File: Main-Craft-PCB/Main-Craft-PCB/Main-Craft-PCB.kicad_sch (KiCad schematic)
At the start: 220 parts, among them J1 Conn_01x10, J1 UART_1, J10 SOL_2, J11 PWR_IN, J12 SOL_3, J13 SOL_4, J15 VESC_1, J16 VESC_2, J17 VESC_3, J18 VESC_4, J19 S500_1, J2 UART_2, J20 S500_2, J21 S500_3, J22 S500_4, J23 LEDS, J24 LEDS, J25 LEDS, J26 LEDS, J3 UART_3, J4 UART_4, J5 RELAY_1, J6 RELAY_2, J7 RELAY_3, J8 RELAY_3, J9 SOL_1, Q1 TIP120, Q10 S9013, Q11 S9013, Q12 S9013, Q13 S9013, Q14 S9013, Q16 S9013, Q2 TIP120, Q25 IRFR9014PBF, Q3 TIP120, Q4 TIP120, Q5 S9013, Q6 S9013, Q7 S9013, Q8 S9013, Q9 S9013, U10 BFU590GX, U10 ZLDO1117G50TA, U2 NUCLEO144-F429ZI, U3 ESP8266, U4 LM358DR2G, U4 SN74LV4052, U5 74HC14, U5 LM358, U8 Pi Pico, U9 74HC14, U9 ZSR330GTA

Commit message: Finish add all footprints and components
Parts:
- AS_DEC_SW1: footprint My_library:1Ms1T1B1M1QE -> My_library:JS202011SCQN
- C1: footprint (none) -> Capacitor_SMD:CP_Elec_10x10.5
- C28, C29, C33, C34: value C -> 100nF; footprint (none) -> Capacitor_SMD:C_0603_1608Metric
- D11, D12, D19, D20, D21, D22, D23, D24: value BLUE -> RED
- D28: value BLUE -> GREEN
- D29: value BLUE -> YELLOW
- D_UP1: footprint Button_Switch_SMD:SW_Push_1P1T_NO_6x6mm_H9.5mm -> My_library:12AWG_PWR_IN
- J1, J2, J3, J4: footprint (none) -> My_library:Conn_01x04_MOLEX
- J10, J12, J13, J15, J16, J17, J18, J19, J20, J21, J22, J5, J6, J7, J8, J9: footprint (none) -> My_library:Conn_01x03_MOLEX
- J11: footprint (none) -> My_library:12AWG_PWR_IN
- J23, J24, J25, J26: footprint (none) -> Connector_PinHeader_2.54mm:PinHeader_1x02_P2.54mm_Vertical
- R33, R34, R43, R44, R47, R48, R51, R52, R86: value 1K -> 150R
- R61: value 1K -> 2K2
- RV10, RV11, RV12, RV9: value R_POT -> 20K; footprint (none) -> My_library:Variable_Resistor
- U2: footprint My_library:MODULE_NUCLEO-F429ZI_JUST_PINS -> My_library:MODULE_NUCLEO-F429ZI
- U3: footprint (none) -> My_library:ESP-8266
- U4: footprint (none) -> Package_SO:SOIC-16_4.55x10.3mm_P1.27mm
- U5: value LM358 -> LM358DR2G; footprint (none) -> Package_SO:SOP-8_3.76x4.96mm_P1.27mm
- U8: footprint (none) -> My_library:Pi_Pico
- U9: footprint (none) -> Package_SO:SO-14_3.9x8.65mm_P1.27mm
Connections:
- net +12V: now also U2.24 (VIN)
- net RESET: now also U2.14 (~{RST})
- removed net LED_1: R25.2, R26.2, R41.2, R42.2, R45.2, R46.2, R49.2, R50.2
- removed net TRIM_POT_?: C28.1, C29.1, C33.1, C34.1, RV10.2, RV11.2, RV12.2, RV9.2
- new net SENS_1: R25.2
- new net SENS_2: R41.2
- new net SENS_3: R45.2
- new net SENS_4: R49.2
- new net SENS_5: R26.2
- new net SENS_6: R42.2
- new net SENS_7: R46.2
- new net SENS_8: R50.2
- new net TRIM_POT_1: C28.1, RV9.2
- new net TRIM_POT_2: C33.1, RV11.2
- new net TRIM_POT_3: C29.1, RV10.2
- new net TRIM_POT_4: C34.1, RV12.2
- no-connect marks 51 -> 60
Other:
- moved on the sheet: U3, U8

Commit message: Start PCB Layout Place Most of Components
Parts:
- removed R89: 2K2, Resistor_SMD:R_0603_1608Metric, symbol Device:R
- removed R91: 10K, Resistor_SMD:R_0603_1608Metric, symbol Device:R
- removed RESET1: SW_SPST, Button_Switch_SMD:SW_Push_1P1T_NO_6x6mm_H9.5mm, symbol Switch:SW_SPST
- D_UP1: footprint My_library:12AWG_PWR_IN -> Button_Switch_SMD:SW_Push_1P1T_NO_6x6mm_H9.5mm
- J1: footprint Connector_PinHeader_1.27mm:PinHeader_1x10_P1.27mm_Vertical -> Connector_PinSocket_2.54mm:PinSocket_1x10_P2.54mm_Vertical
- J10, J12, J13, J9: footprint My_library:Conn_01x03_MOLEX -> My_library:Conn_01x02_MOLEX
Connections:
- net BTN_1: now also U2.38 (PC0)
- net BTN_2: now also U2.45 (PD7)
- net BTN_3: now also U2.43 (PD6)
- net BTN_4: now also U2.41 (PD5)
- net BTN_5: now also U2.39 (PD4)
- net BTN_6: now also U2.40 (PD3)
- net CLK_1: now also U2.11 (PF7)
- net CLK_2: now also U2.46 (PE2)
- net CON_INPUT: now also U2.114 (PF10)
- net DEBUG_1: now also U2.121 (PE12)
- net DEBUG_2: now also U2.123 (PE14)
- net DEBUG_3: now also U2.125 (PE15)
- net I2C_ESP_SCl: now also U2.75 (PB8)
- net I2C_ESP_SDA: now also U2.77 (PB9)
- net I2C_PICO_SCl: now also U2.97 (PB10)
- net I2C_PICO_SDA: now also U2.90 (PB11)
- net LOW_VOLT_1: now also U2.94 (PB2)
- net LOW_VOLT_2: now also U2.117 (PD11)
- net LOW_VOLT_3: now also U2.28 (ETH_REF_CLK/PA0)
- net LOW_VOLT_4: now also U2.136 (PE0)
- net MISO_1: now also U2.56 (PF9)
- net MISO_2: now also U2.50 (PE5)
- net MOSI_1: now also U2.54 (PF8)
- net MOSI_2: now also U2.62 (PE6)
- net RELAY_1: now also U2.52 (PF2)
- net RELAY_2: now also U2.57 (PD0)
- net RELAY_3: now also U2.55 (PD1)
- net RELAY_4: now also U2.59 (PG0)
- net S500_1: now also U2.96 (PB1)
- net S500_2: now also U2.89 (PB6)
- net S500_3: now also U2.113 (PD13)
- net S500_4: now also U2.115 (PD12)
- net SENS_1: now also U2.131 (PF12)
- net SENS_2: now also U2.129 (PF13)
- net SENS_3: now also U2.124 (PE9)
- net SENS_4: now also U2.128 (PE11)
- net SENS_5: now also U2.122 (PF14)
- net SENS_6: now also U2.127 (PE13)
- net SENS_7: now also U2.132 (PF15)
- net SENS_8: now also U2.133 (PG14)
- net SOL_1: now also U2.63 (PG9)
- net SOL_2: now also U2.112 (PE8)
- net SOL_3: now also U2.116 (PE7)
- net SOL_4: now also U2.119 (PE10)
- net SW_1_DOWN: now also U2.2 (PC11)
- net SW_1_UP: now also U2.1 (PC10)
- net SW_2_DOWN: now also U2.4 (PD2)
- net SW_2_UP: now also U2.3 (PC12)
- net SW_3_DOWN: now also U2.44 (PG3)
- net SW_3_UP: now also U2.42 (PG2)
- net TRIM_POT_1: now also U2.32 (PA4)
- net TRIM_POT_2: now also U2.83 (PA5)
- net TRIM_POT_3: now also U2.85 (PA6)
- net TRIM_POT_4: now also U2.87 (ETH_CRS_DV/PA7)
- net VESC_1: now also U2.109 (PA3)
- net VESC_2: now also U2.74 (PC8)
- net VESC_3: now also U2.73 (PC9)
- net VESC_4: now also U2.99 (PB4)
- no-connect marks 60 -> 116
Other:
- moved on the sheet: D11, D12, D19, D20, D21, D22, D23, D24, Q10, Q11, Q12, Q5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

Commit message: Continue PCB
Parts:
- added J23: BAT_IN, My_library:Conn_01x04_MOLEX, symbol Connector_Generic:Conn_01x04
- renumbered C28 to C26, C29 to C27, C33 to C31, C34 to C32, C1 to C36, J20 to J10, J21 to J11, J22 to J12, J9 to J13, J10 to J14, J5 to J15, J6 to J16, J7 to J17, J8 to J18, J12 to J19, J13 to J20, J11 to J21, J15 to J24, J16 to J25, J17 to J26, J18 to J27, J23 to J5, J24 to J6, J25 to J7, J26 to J8, J19 to J9, R3 to R1, R4 to R2, R25 to R24, R26 to R25, R33 to R32, R34 to R33, R2 to R40, R58 to R57, R60 to R58, R61 to R59, R63 to R61, R64 to R62, U8 to U2, U9 to U8
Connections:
- net BATT_1_IN: now also J23.1 (Pin_1)
- net BATT_2_IN: now also J23.2 (Pin_2)
- net BATT_3_IN: now also J23.3 (Pin_3)
- net BATT_4_IN: now also J23.4 (Pin_4)

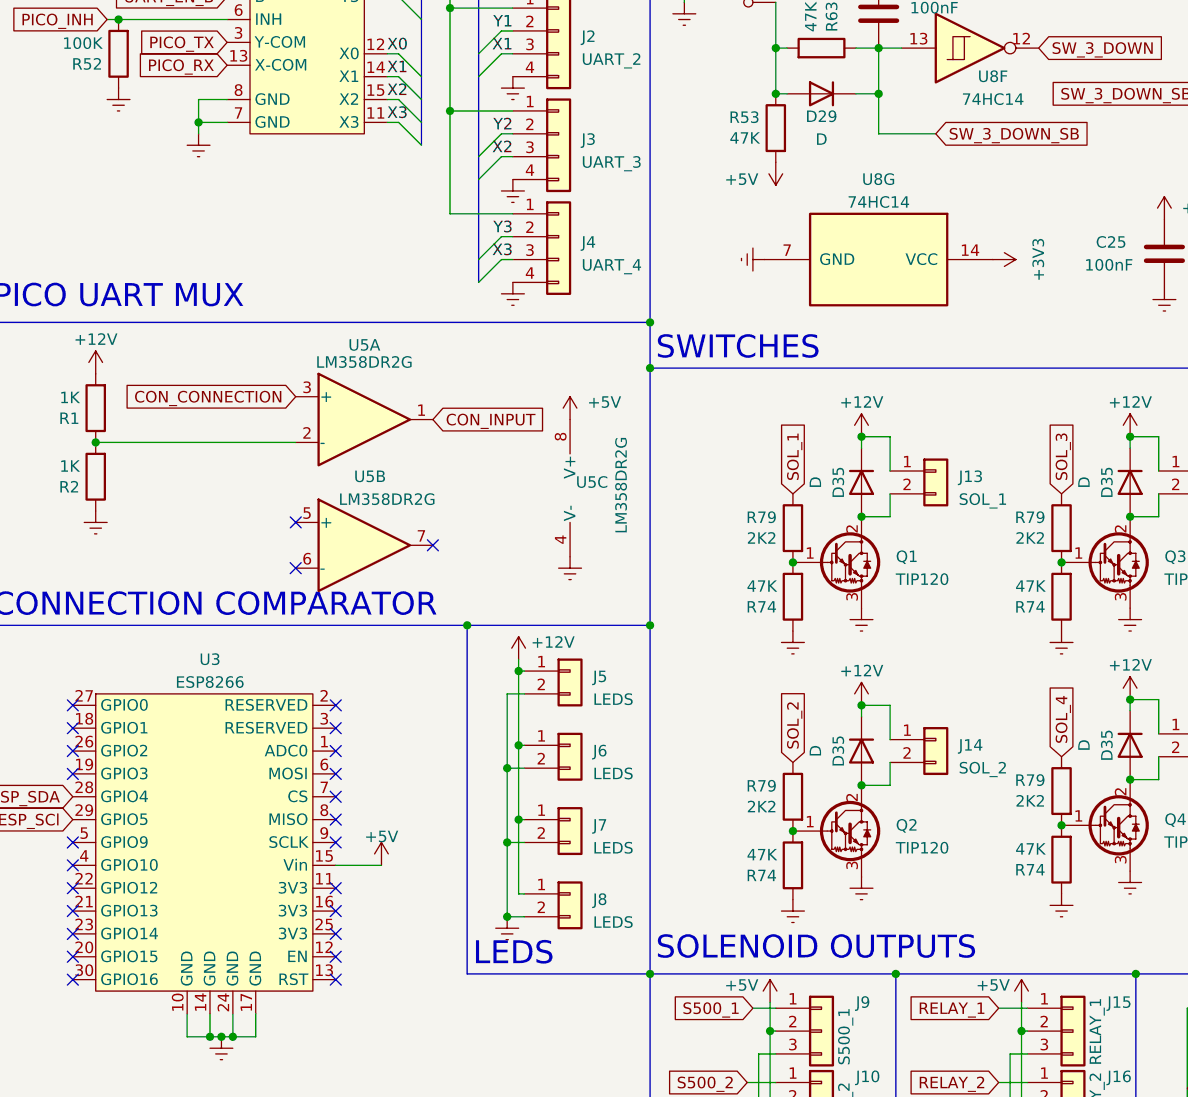
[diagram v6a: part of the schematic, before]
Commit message: Fix PCB schematic issues - start PCB again
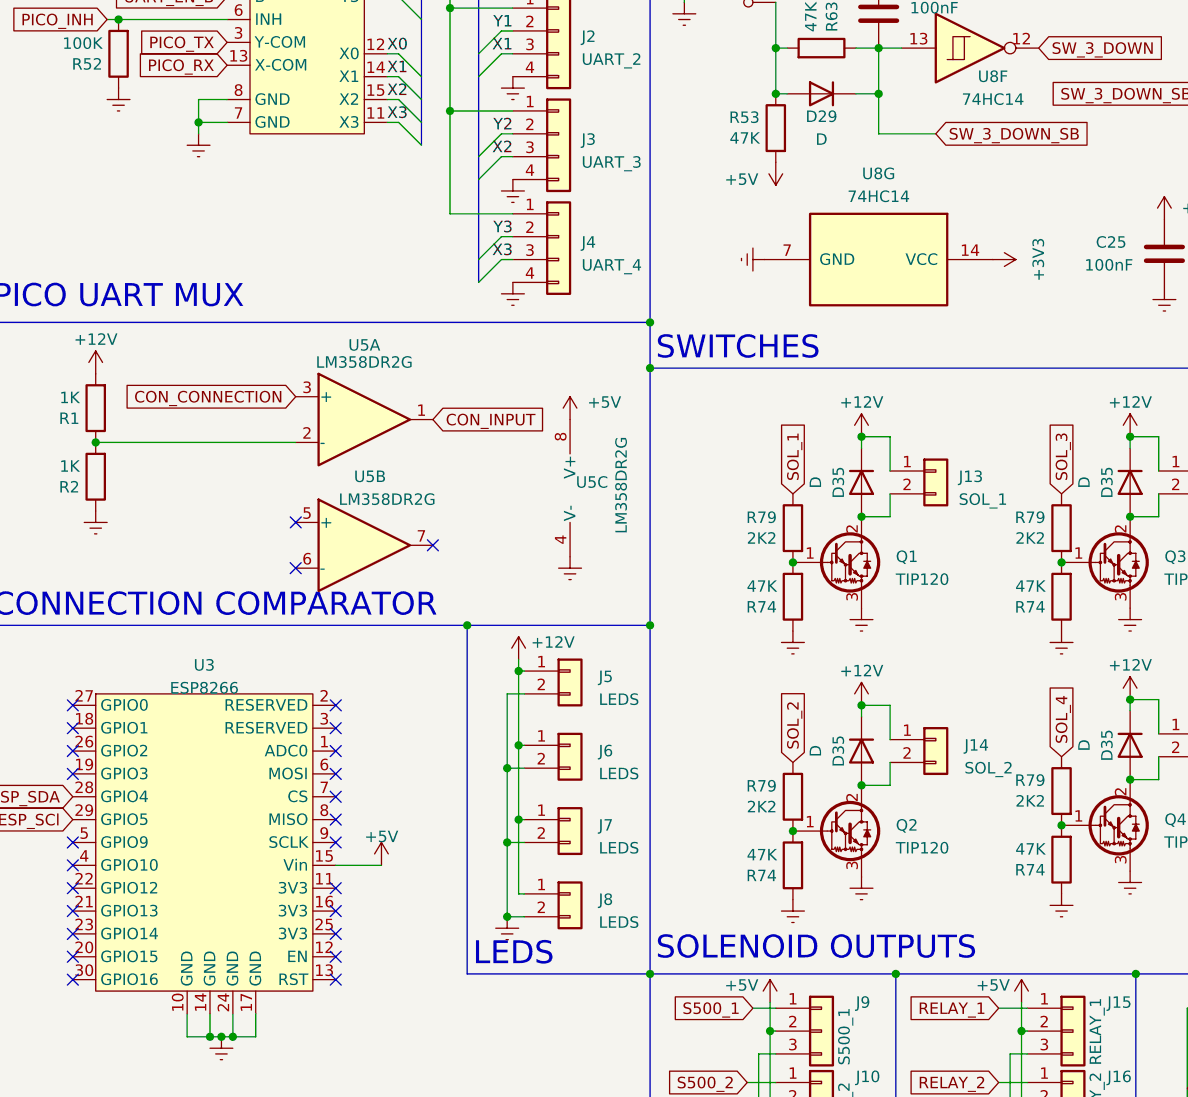
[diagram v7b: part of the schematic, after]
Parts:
- U2: footprint My_library:Pi_Pico -> My_library:pi_pico
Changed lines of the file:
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@@
   (symbol (lib_id "My_Library.lib:ESP8266") (at 134.62 226.695 0) (unit 1)
     (in_bom yes) (on_board yes) (dnp no) (fields_autoplaced)
-    (property "Reference" "U3" (at 134.62 210.185 0)
+    (property "Reference" "U3" (at 133.985 210.82 0)
       (effects (font (size 1.27 1.27)))
     )
-    (property "Value" "ESP8266" (at 134.62 212.725 0)
+    (property "Value" "ESP8266" (at 133.985 213.36 0)
       (effects (font (size 1.27 1.27)))
     )
@@
   (symbol (lib_id "Connector_Generic:Conn_01x02") (at 174.625 211.455 0) (unit 1)
     (in_bom yes) (on_board yes) (dnp no) (fields_autoplaced)
-    (property "Reference" "J5" (at 177.165 212.09 0)
+    (property "Reference" "J5" (at 177.8 212.09 0)
       (effects (font (size 1.27 1.27)) (justify left))
     )
-    (property "Value" "LEDS" (at 177.165 214.63 0)
+    (property "Value" "LEDS" (at 177.8 214.63 0)
       (effects (font (size 1.27 1.27)) (justify left))
     )
@@
   (symbol (lib_id "Connector_Generic:Conn_01x02") (at 174.625 227.965 0) (unit 1)
     (in_bom yes) (on_board yes) (dnp no) (fields_autoplaced)
-    (property "Reference" "J7" (at 177.165 228.6 0)
+    (property "Reference" "J7" (at 177.8 228.6 0)
       (effects (font (size 1.27 1.27)) (justify left))
     )
-    (property "Value" "LEDS" (at 177.165 231.14 0)
+    (property "Value" "LEDS" (at 177.8 231.14 0)
       (effects (font (size 1.27 1.27)) (justify left))
     )
@@
       (effects (font (size 1.27 1.27)))
     )
-    (property "Footprint" "My_library:Pi_Pico" (at 52.07 238.125 0)
+    (property "Footprint" "My_library:pi_pico" (at 52.07 238.125 0)
       (effects (font (size 1.27 1.27)) hide)
     )
@@
   (symbol (lib_id "Connector_Generic:Conn_01x02") (at 174.625 219.71 0) (unit 1)
     (in_bom yes) (on_board yes) (dnp no) (fields_autoplaced)
-    (property "Reference" "J6" (at 177.165 220.345 0)
+    (property "Reference" "J6" (at 177.8 220.345 0)
       (effects (font (size 1.27 1.27)) (justify left))
     )
-    (property "Value" "LEDS" (at 177.165 222.885 0)
+    (property "Value" "LEDS" (at 177.8 222.885 0)
       (effects (font (size 1.27 1.27)) (justify left))
     )
@@
   (symbol (lib_id "Connector_Generic:Conn_01x02") (at 174.625 236.22 0) (unit 1)
     (in_bom yes) (on_board yes) (dnp no) (fields_autoplaced)
-    (property "Reference" "J8" (at 177.165 236.855 0)
+    (property "Reference" "J8" (at 177.8 236.855 0)
       (effects (font (size 1.27 1.27)) (justify left))
     )
-    (property "Value" "LEDS" (at 177.165 239.395 0)
+    (property "Value" "LEDS" (at 177.8 239.395 0)
       (effects (font (size 1.27 1.27)) (justify left))
     )
@@
   (symbol (lib_id "74xx:74HC14") (at 208.915 165.735 270) (unit 7)
     (in_bom yes) (on_board yes) (dnp no) (fields_autoplaced)
-    (property "Reference" "U8" (at 208.915 156.845 90)
+    (property "Reference" "U8" (at 208.915 156.21 90)
       (effects (font (size 1.27 1.27)))
     )
-    (property "Value" "74HC14" (at 208.915 159.385 90)
+    (property "Value" "74HC14" (at 208.915 158.75 90)
       (effects (font (size 1.27 1.27)))
     )
@@
   (symbol (lib_id "Connector_Generic:Conn_01x02") (at 215.265 219.075 0) (unit 1)
     (in_bom yes) (on_board yes) (dnp no) (fields_autoplaced)
-    (property "Reference" "J14" (at 217.805 219.71 0)
+    (property "Reference" "J14" (at 218.44 219.71 0)
       (effects (font (size 1.27 1.27)) (justify left))
     )
-    (property "Value" "SOL_2" (at 217.805 222.25 0)
+    (property "Value" "SOL_2" (at 218.44 222.25 0)
       (effects (font (size 1.27 1.27)) (justify left))
     )

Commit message: finish component placement and start traces
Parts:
- removed C27 (x2): 100nF, Capacitor_SMD:C_0603_1608Metric, symbol Device:C
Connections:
- net Y4 is gone; now on net Y3: U4.4 (Y3)
- net +12V: now also J1.1 (Pin_1)
- net +3V3: now also R52.2, R52.2, R52.2, R53.2, R53.2, R53.2, R69.2, R70.2, R71.2, R72.2, R73.2, R74.2
- net +5V: no longer R52.2, R52.2, R52.2, R53.2, R53.2, R53.2, R69.2, R70.2, R71.2, R72.2, R73.2, R74.2
- net BATT_1_IN: now also J23.4 (Pin_4); no longer J23.1 (Pin_1)
- net BATT_2_IN: now also J23.3 (Pin_3); no longer J23.2 (Pin_2)
- net BATT_3_IN: now also J23.2 (Pin_2); no longer J23.3 (Pin_3)
- net BATT_4_IN: now also J23.1 (Pin_1); no longer J23.4 (Pin_4)
- net VESC_1: now also J24.1 (Pin_1); no longer J24.2 (Pin_2)
- net VESC_2: now also J25.1 (Pin_1); no longer J25.2 (Pin_2)
- net VESC_3: now also J26.1 (Pin_1); no longer J26.2 (Pin_2)
- net VESC_4: now also J27.1 (Pin_1); no longer J27.2 (Pin_2)
- net VIN: no longer J1.1 (Pin_1)
- removed net VESC_IN_5V: J24.1 (Pin_1), J25.1 (Pin_1), J26.1 (Pin_1), J27.1 (Pin_1)
- no-connect marks 116 -> 120
